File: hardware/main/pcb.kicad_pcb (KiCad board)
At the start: 2 copper layers, 42 x 42 mm, 11 parts, among them J3 Conn_01x03_Socket

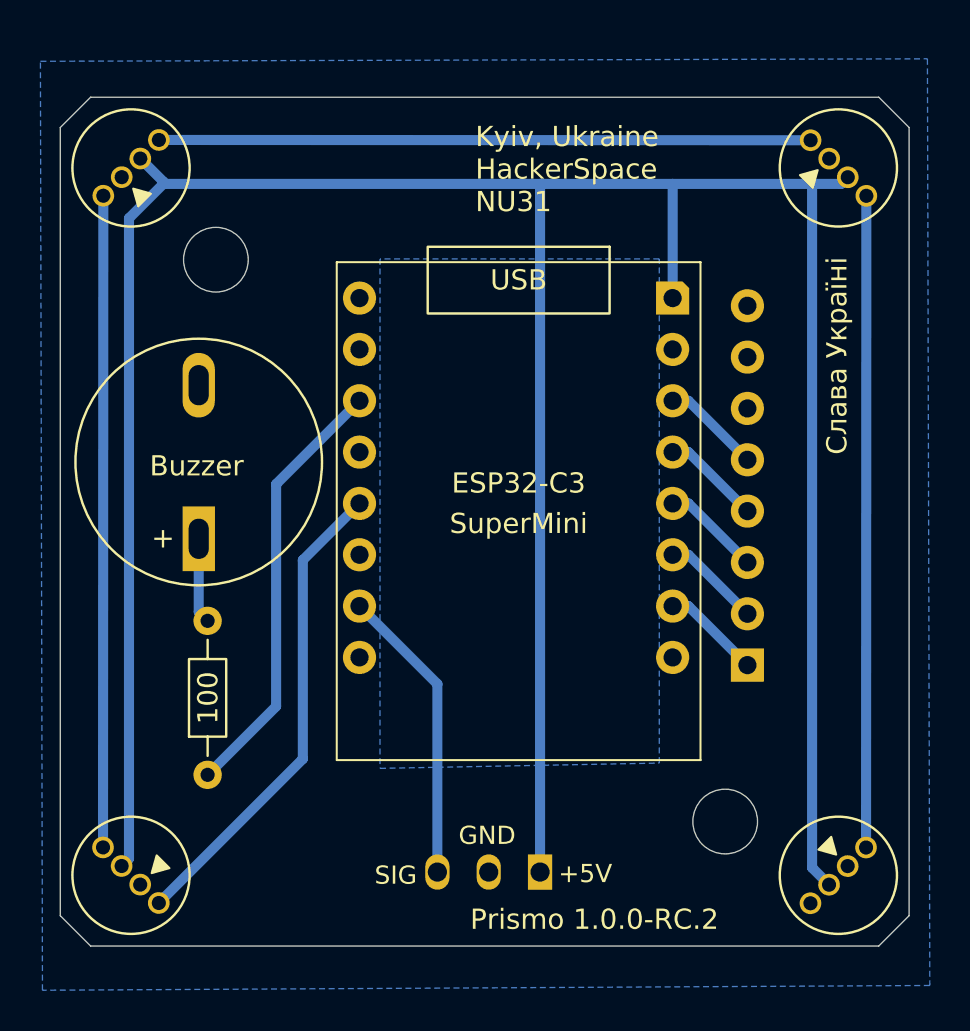
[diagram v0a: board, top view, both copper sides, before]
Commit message: Add 100uF bulk capacitors on 3.3V and 5V rails
- Add C1 (100uF) between 3.3V and GND next to the PN532 VCC/GND pins
- Add C2 (100uF) on the +5V input near the J3 connector
- Add C_Polarized symbol and CP_Radial_D5.0mm_P2.00mm footprint to the prismo library

Known issue: J3 GND pad is cut off from the GND pour by the new C2 +5V track.

Co-Authored-By: Claude Opus 5.5 (1M context) <noreply@anthropic.com>
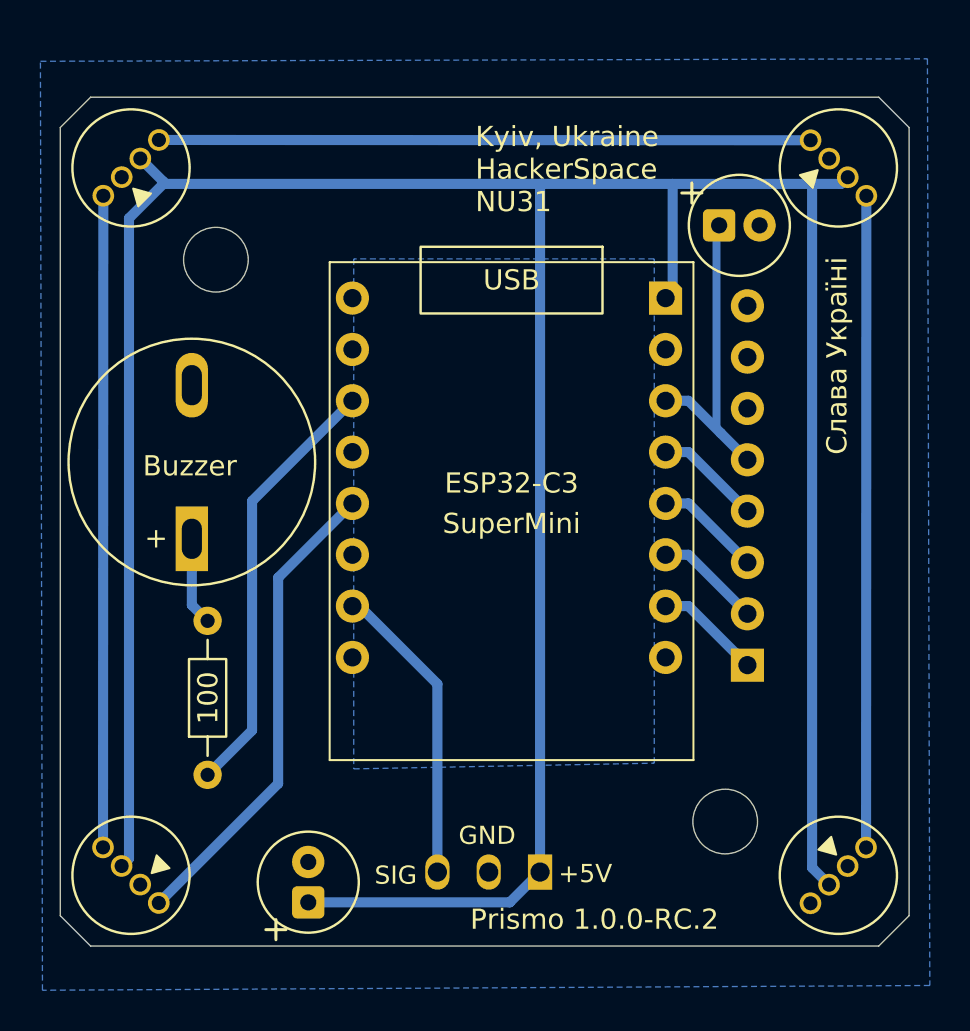
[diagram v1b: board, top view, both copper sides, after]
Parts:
- added C1: 100uF, prismo:CP_Radial_D5.0mm_P2.00mm, F.Cu at (139.7, 52.0)
- added C2: 100uF, prismo:CP_Radial_D5.0mm_P2.00mm, F.Cu at (119.4, 85.5)
- moved U1 0.35 mm to (129.4, 65.8)
- moved BZ1 0.34 mm to (113.6, 67.5)
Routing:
- net +5V: track 145.1 -> 157.2 mm
- net Net-(U1-3V3): track 4.91 -> 15.3 mm
